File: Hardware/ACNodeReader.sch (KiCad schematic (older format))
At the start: 36 parts, among them J1 8P8C, J2 AVR-ISP-6, J3 Conn_01x04_Female, J4 Conn_01x03_Male, J5 Conn_01x04_Female, J6 Conn_01x03_Male, J7 Conn_01x05_Male, J8 Conn_01x03_Male, SW1 SW_Push, SW2 SW_Push, U1 L78L05_SOT89, U2 ATmega88-20AU, U3 ISL8489EIBZ, U4 SI7060-B-00-IV, Y1 16MHz

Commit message: Update a component value
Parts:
- R11: value R -> 10K
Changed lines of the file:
@@
 P 3650 6000
 F 0 "R11" V 3443 6000 50  0000 C CNN
-F 1 "R" V 3534 6000 50  0000 C CNN
+F 1 "10K" V 3534 6000 50  0000 C CNN
 F 2 "Resistor_SMD:R_0603_1608Metric" V 3580 6000 50  0001 C CNN
 F 3 "~" H 3650 6000 50  0001 C CNN

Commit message: Random locl changes
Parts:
- removed J4, J6, J8: Conn_01x03_Male, Connector_PinHeader_2.54mm:PinHeader_1x03_P2.54mm_Vertical, symbol Connector:Conn_01x03_Male
- removed J7: Conn_01x05_Male, Connector_PinHeader_2.54mm:PinHeader_1x05_P2.54mm_Vertical, symbol Connector:Conn_01x05_Male
- removed R10, R8, R9: 220R, Resistor_SMD:R_0603_1608Metric, symbol Device:R
- removed SW1: SW_Push, Button_Switch_THT:SW_PUSH_6mm, symbol Switch:SW_Push
- removed U2: ATmega88-20AU, Package_QFP:TQFP-32_7x7mm_P0.8mm, symbol MCU_Microchip_ATmega:ATmega88-20AU
- removed Y1: 16MHz, Crystal:Crystal_SMD_HC49-SD, symbol Device:Crystal_Small
- added U2: ATmega88PB-AU, Package_QFP:TQFP-32_7x7mm_P0.8mm, symbol MCU_Microchip_ATmega:ATmega88PB-AU
- added Y1: Crystal_GND24, Crystal:Crystal_SMD_Abracon_ABM3B-4Pin_5.0x3.2mm, symbol Device:Crystal_GND24
- J2: footprint Connector_IDC:IDC-Header_2x03_P2.54mm_Vertical -> Tag-Connect:TC2030-MCP
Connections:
- wire segments 189 -> 157
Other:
- note removed: "I2C Debug"
- note removed: "Power Debug"
- note removed: "Reset Switch"
- note removed: "SPI debug"
- note removed: "Serial Debug"

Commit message: Toying with the circuit a bit
Removed the capacitor across reset since it breaks DebugWire which
is worth having usable because it helps when all hell breaks loose :-)

Added zero ohm links for switching LED from common anode to common cathode

Switched capacitors to (much smaller) MLCC variants in preparation for attempting
to cram everything into a smaller board
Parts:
- removed C1, C2: 470u, Capacitor_SMD:CP_Elec_8x10, symbol Device:CP
- removed C7: 4.7nF, Capacitor_SMD:C_0603_1608Metric, symbol Device:C
- added C1, C2: 10u, Capacitor_SMD:C_0805_2012Metric, symbol Device:C
- added R8: DNF, Resistor_SMD:R_0603_1608Metric, symbol Device:R
- added R9: 0R, Resistor_SMD:R_0603_1608Metric, symbol Device:R
- J2: symbol Connector:AVR-ISP-6 -> ACNodeReader-rescue:AVR-ISP-6-Connector
- U2: symbol MCU_Microchip_ATmega:ATmega88PB-AU -> ACNodeReader-rescue:ATmega88PB-AU-MCU_Microchip_ATmega
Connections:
- wire segments 157 -> 158
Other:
- moved on the sheet: R4
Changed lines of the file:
@@
 EESchema Schematic File Version 4
-LIBS:ACNodeReader-cache
-EELAYER 29 0
+EELAYER 30 0
 EELAYER END
 $Descr A4 11693 8268
@@
 Wire Wire Line
 	2050 1800 2050 1500
-$Comp
-L Device:CP C1
-U 1 1 5D3DABEB
-P 1300 1350
-F 0 "C1" H 1418 1396 50  0000 L CNN
-F 1 "470u" H 1418 1305 50  0000 L CNN
-F 2 "Capacitor_SMD:CP_Elec_8x10" H 1338 1200 50  0001 C CNN
-F 3 "~" H 1300 1350 50  0001 C CNN
-	1    1300 1350
-	1    0    0    -1
-$EndComp
-$Comp
-L Device:CP C2
-U 1 1 5D3DC471
-P 2750 1350
-F 0 "C2" H 2868 1396 50  0000 L CNN
-F 1 "470u" H 2868 1305 50  0000 L CNN
-F 2 "Capacitor_SMD:CP_Elec_8x10" H 2788 1200 50  0001 C CNN
-F 3 "~" H 2750 1350 50  0001 C CNN
-	1    2750 1350
-	1    0    0    -1
-$EndComp
 Wire Wire Line
 	2750 1200 2750 1150
@@
 L power:+5V #PWR0112
 U 1 1 5D3FCC1C
-P 5350 3400
-F 0 "#PWR0112" H 5350 3250 50  0001 C CNN
-F 1 "+5V" H 5450 3450 50  0000 C CNN
-F 2 "" H 5350 3400 50  0001 C CNN
-F 3 "" H 5350 3400 50  0001 C CNN
-	1    5350 3400
+P 5650 3850
+F 0 "#PWR0112" H 5650 3700 50  0001 C CNN
+F 1 "+5V" H 5750 3900 50  0000 C CNN
+F 2 "" H 5650 3850 50  0001 C CNN
+F 3 "" H 5650 3850 50  0001 C CNN
+	1    5650 3850
 	1    0    0    -1
 $EndComp
@@
 $EndComp
 Wire Wire Line
-	6150 3800 6050 3800
+	6150 3800 6100 3800
 $Comp
 L Device:C C5
@@
 L Device:R R4
 U 1 1 5D47849B
-P 5350 3700
-F 0 "R4" H 5420 3746 50  0000 L CNN
-F 1 "10k" H 5420 3655 50  0000 L CNN
-F 2 "Resistor_SMD:R_0805_2012Metric" V 5280 3700 50  0001 C CNN
-F 3 "~" H 5350 3700 50  0001 C CNN
-	1    5350 3700
-	1    0    0    -1
-$EndComp
-Wire Wire Line
-	5350 3950 5350 3850
-Wire Wire Line
-	5350 3550 5350 3400
+P 5500 3950
+F 0 "R4" H 5570 3996 50  0000 L CNN
+F 1 "10k" H 5570 3905 50  0000 L CNN
+F 2 "Resistor_SMD:R_0805_2012Metric" V 5430 3950 50  0001 C CNN
+F 3 "~" H 5500 3950 50  0001 C CNN
+	1    5500 3950
+	0    1    1    0
+$EndComp
 Wire Wire Line
 	5100 3000 5100 2800
@@
 	5750 2800 5750 2950
 Wire Wire Line
-	5750 2950 6050 2950
-Wire Wire Line
-	6050 2950 6050 3800
+	6100 2950 6100 3800
 Connection ~ 5750 2950
 Wire Wire Line
 	5750 2950 5750 3150
-Connection ~ 6050 3800
-Wire Wire Line
-	6050 3800 5900 3800
-Wire Wire Line
-	5450 3950 5350 3950
-Connection ~ 5350 3950
-Wire Wire Line
-	5750 3950 5750 3800
-Wire Wire Line
-	5750 3800 5900 3800
 Connection ~ 5900 3800
 $Comp
-L Device:C C7
-U 1 1 5D4A17E0
-P 5600 3950
-F 0 "C7" V 5450 3950 50  0000 C CNN
-F 1 "4.7nF" V 5750 3950 50  0000 C CNN
-F 2 "Capacitor_SMD:C_0603_1608Metric" H 5638 3800 50  0001 C CNN
-F 3 "~" H 5600 3950 50  0001 C CNN
-	1    5600 3950
-	0    1    1    0
-$EndComp
-$Comp
-L Connector:AVR-ISP-6 J2
+L ACNodeReader-rescue:AVR-ISP-6-Connector J2
 U 1 1 5D4A869B
 P 5300 2100
@@
 U 1 1 5D569267
 P 5150 3450
-F 0 "J5" H 5178 3426 50  0000 L CNN
-F 1 "Conn_01x04_Female" H 5178 3335 50  0000 L CNN
+F 0 "J5" H 5150 3300 50  0000 L CNN
+F 1 "Conn_01x04_Female" H 4850 3200 50  0000 L CNN
 F 2 "Connector_PinHeader_2.54mm:PinHeader_1x04_P2.54mm_Vertical" H 5150 3450 50  0001 C CNN
 F 3 "~" H 5150 3450 50  0001 C CNN
@@
 	4150 3600 4350 3600
 Wire Wire Line
-	5900 3250 5900 3800
+	5900 3250 5900 3400
 Wire Wire Line
 	4950 3450 4850 3450
@@
 	2350 1150 2750 1150
 $Comp
-L MCU_Microchip_ATmega:ATmega88PB-AU U2
+L ACNodeReader-rescue:ATmega88PB-AU-MCU_Microchip_ATmega U2
 U 1 1 5D98CB6F
 P 3450 3650
@@
 $EndComp
 Wire Wire Line
-	4850 3250 5900 3250
+	4850 3250 5700 3250
 Wire Wire Line
 	4050 3050 4300 3050
@@
 Wire Wire Line
 	4350 3100 4750 3100
+Wire Wire Line
+	5650 3950 5650 3850
+$Comp
+L Device:R R9
+U 1 1 5EE364C3
+P 5900 3550
+F 0 "R9" H 5830 3504 50  0000 R CNN
+F 1 "0R" H 5830 3595 50  0000 R CNN
+F 2 "Resistor_SMD:R_0603_1608Metric" V 5830 3550 50  0001 C CNN
+F 3 "~" H 5900 3550 50  0001 C CNN
+	1    5900 3550
+	-1   0    0    1
+$EndComp
+Wire Wire Line
+	5900 3700 5900 3800
+$Comp
+L Device:R R8
+U 1 1 5EE3ACF5
+P 5700 3550
+F 0 "R8" H 5550 3600 50  0000 L CNN
+F 1 "DNF" H 5500 3500 50  0000 L CNN
+F 2 "Resistor_SMD:R_0603_1608Metric" V 5630 3550 50  0001 C CNN
+F 3 "~" H 5700 3550 50  0001 C CNN
+	1    5700 3550
+	1    0    0    -1
+$EndComp
+Wire Wire Line
+	5700 3400 5700 3250
+Connection ~ 5700 3250
+Wire Wire Line
+	5700 3250 5900 3250
+Wire Wire Line
+	5700 3700 5700 3950
+Wire Wire Line
+	5700 3950 5650 3950
+Connection ~ 5650 3950
+Connection ~ 6100 3800
+Wire Wire Line
+	5900 3800 6100 3800
+Wire Wire Line
+	5750 2950 6100 2950
+$Comp
+L Device:C C1
+U 1 1 5EE74DE3
+P 1300 1350
+F 0 "C1" H 1415 1396 50  0000 L CNN
+F 1 "10u" H 1415 1305 50  0000 L CNN
+F 2 "Capacitor_SMD:C_0805_2012Metric" H 1338 1200 50  0001 C CNN
+F 3 "~" H 1300 1350 50  0001 C CNN
+	1    1300 1350
+	1    0    0    -1
+$EndComp
+$Comp
+L Device:C C2
+U 1 1 5EE7545C
+P 2750 1350
+F 0 "C2" H 2865 1396 50  0000 L CNN
+F 1 "10u" H 2865 1305 50  0000 L CNN
+F 2 "Capacitor_SMD:C_0805_2012Metric" H 2788 1200 50  0001 C CNN
+F 3 "~" H 2750 1350 50  0001 C CNN
+	1    2750 1350
+	1    0    0    -1
+$EndComp
 $EndSCHEMATC

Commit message: New, smaller, better PCB design
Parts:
- removed J1: 8P8C, Connector_RJ:RJ45_Amphenol_54602-x08_Horizontal, symbol Connector:8P8C
- removed SW2: SW_Push, Button_Switch_THT:SW_PUSH_6mm, symbol Switch:SW_Push
- removed U4: SI7060-B-00-IV, Package_TO_SOT_SMD:SOT-23-5, symbol ExtraParts:SI7060-B-00-IV
- added D1: D_Zener, Diode_SMD:D_SOD-323F, symbol Device:D_Zener
- added H1, H2: MountingHole, MountingHole:MountingHole_3.2mm_M3_DIN965, symbol Mechanical:MountingHole
- added J1: Conn_01x08_Male, Connector_PinHeader_2.54mm:PinHeader_1x08_P2.54mm_Horizontal, symbol Connector:Conn_01x08_Male
- added J4: Conn_01x02_Male, Connector_PinHeader_2.54mm:PinHeader_1x02_P2.54mm_Horizontal, symbol Connector:Conn_01x02_Male
- added J6: Conn_01x04_Male, Connector_PinHeader_2.54mm:PinHeader_1x04_P2.54mm_Horizontal, symbol Connector:Conn_01x04_Male
- added J7: Conn_01x04_Male, Connector_PinHeader_2.54mm:PinHeader_1x04_P2.54mm_Vertical, symbol Connector:Conn_01x04_Male
- added U4: LM75C, Package_SO:SO-8_3.9x4.9mm_P1.27mm, symbol Sensor_Temperature:LM75C
- J2: footprint Tag-Connect:TC2030-MCP -> Tag-Connect:TC2030-MCP-NL
- J5: footprint Connector_PinHeader_2.54mm:PinHeader_1x04_P2.54mm_Vertical -> Connector_PinHeader_2.54mm:PinHeader_1x04_P2.54mm_Horizontal
- R1, R2, R4: footprint Resistor_SMD:R_0805_2012Metric -> Resistor_SMD:R_0603_1608Metric
- Y1: footprint Crystal:Crystal_SMD_Abracon_ABM3B-4Pin_5.0x3.2mm -> Crystal:Crystal_SMD_7050-4Pin_7.0x5.0mm
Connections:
- net +12V: now also D1.1 (K), J1.4 (Pin_4), J1.5 (Pin_5)
- net +5V: now also R9.1, J6.3 (Pin_3), J7.1 (Pin_1), U4.8 (+Vs); no longer R8.2
- net GND: now also R8.2, D1.2 (A), J1.1 (Pin_1), J1.2 (Pin_2), J6.4 (Pin_4), J7.2 (Pin_2), U4.4 (GND), U4.5 (A2), U4.6 (A1), U4.7 (A0); no longer R9.1
- net RX+: now also J1.8 (Pin_8)
- net RX-: now also J1.7 (Pin_7)
- net TX+: now also J1.6 (Pin_6)
- net TX-: now also J1.3 (Pin_3)
- net i2c_SCL: now also R1.1, J7.3 (Pin_3), U4.2 (SCL); no longer R2.1
- net i2c_SDA: now also R2.1, J7.4 (Pin_4), U4.1 (SDA); no longer R1.1
- net uC_RX: now also J6.2 (Pin_2)
- net uC_TX: now also J6.1 (Pin_1)
- net at U2.23 (PC0): no longer R5.2
- net at U2.24 (PC1): no longer R6.2
- net at U2.25 (PC2): no longer R7.2
- net at C10.2, R11.1: now also J4.2 (Pin_2)
- net at C10.1, U2.11 (PD7): now also J4.1 (Pin_1)
- net LED2: now reaches U2.10 (PD6)
- net LED2: now also R6.2
- net LED3: now reaches U2.13 (PB1)
- net LED3: now also R7.2
- net LED1: now reaches U2.9 (PD5)
- net LED1: now also R5.2
- no-connect marks 1 -> 13
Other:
- note added: "May be TMP1075, PCT2075 or any other LM75-compatible IC"
- moved on the sheet: C9, J5, R1, R2, R5, R6, R7, R8, R9

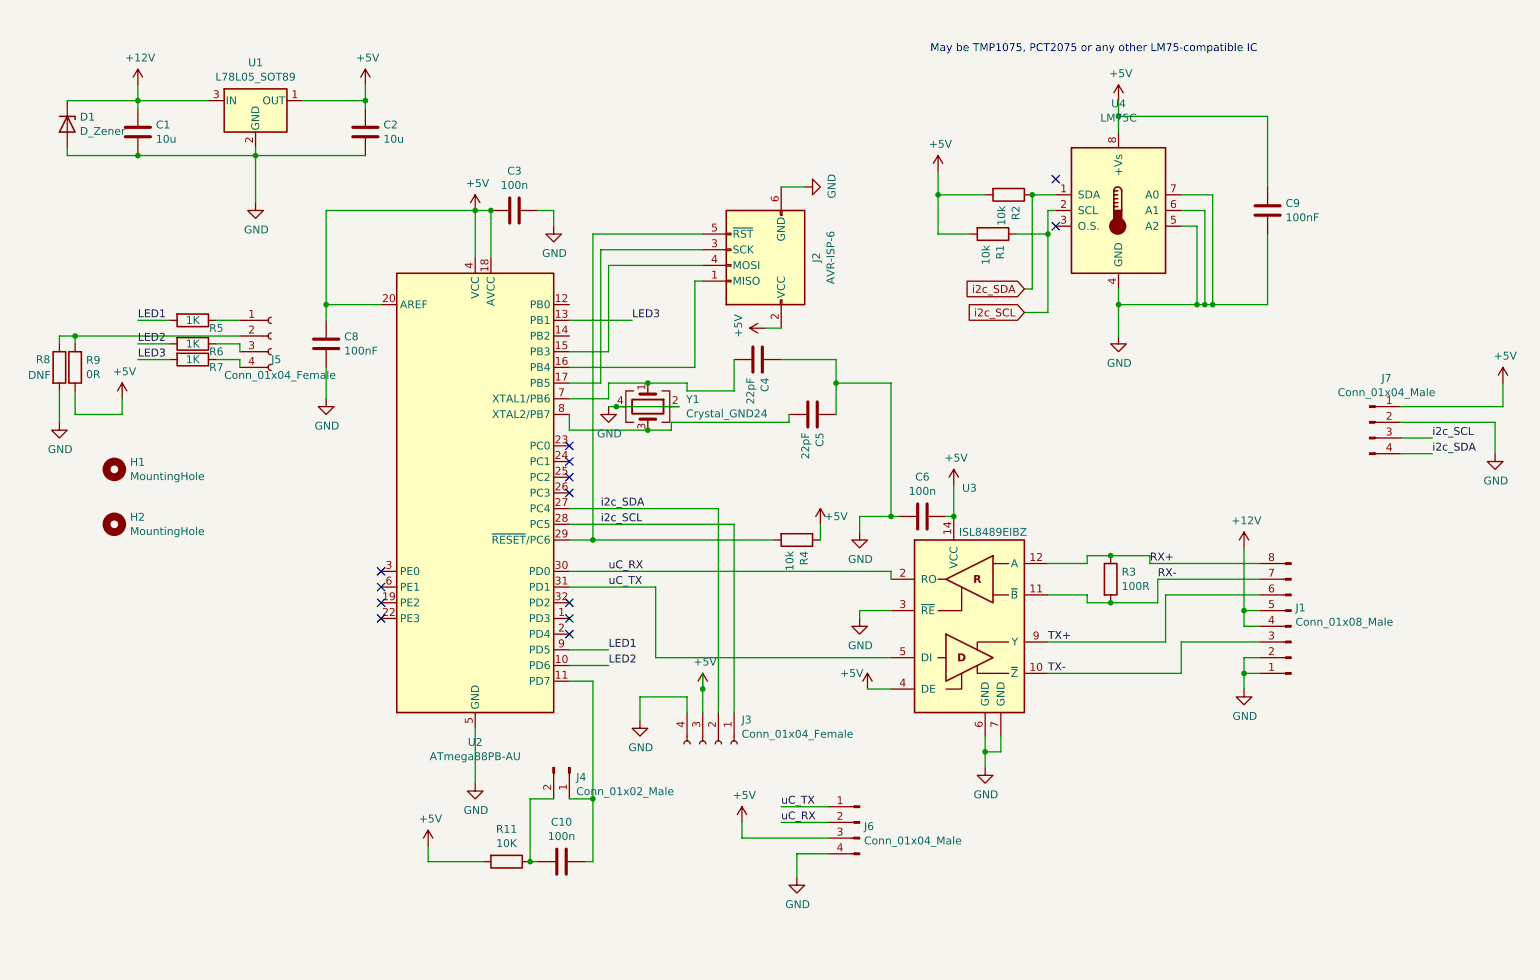
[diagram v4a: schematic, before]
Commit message: Slight schematic changes - mostly text descriptions
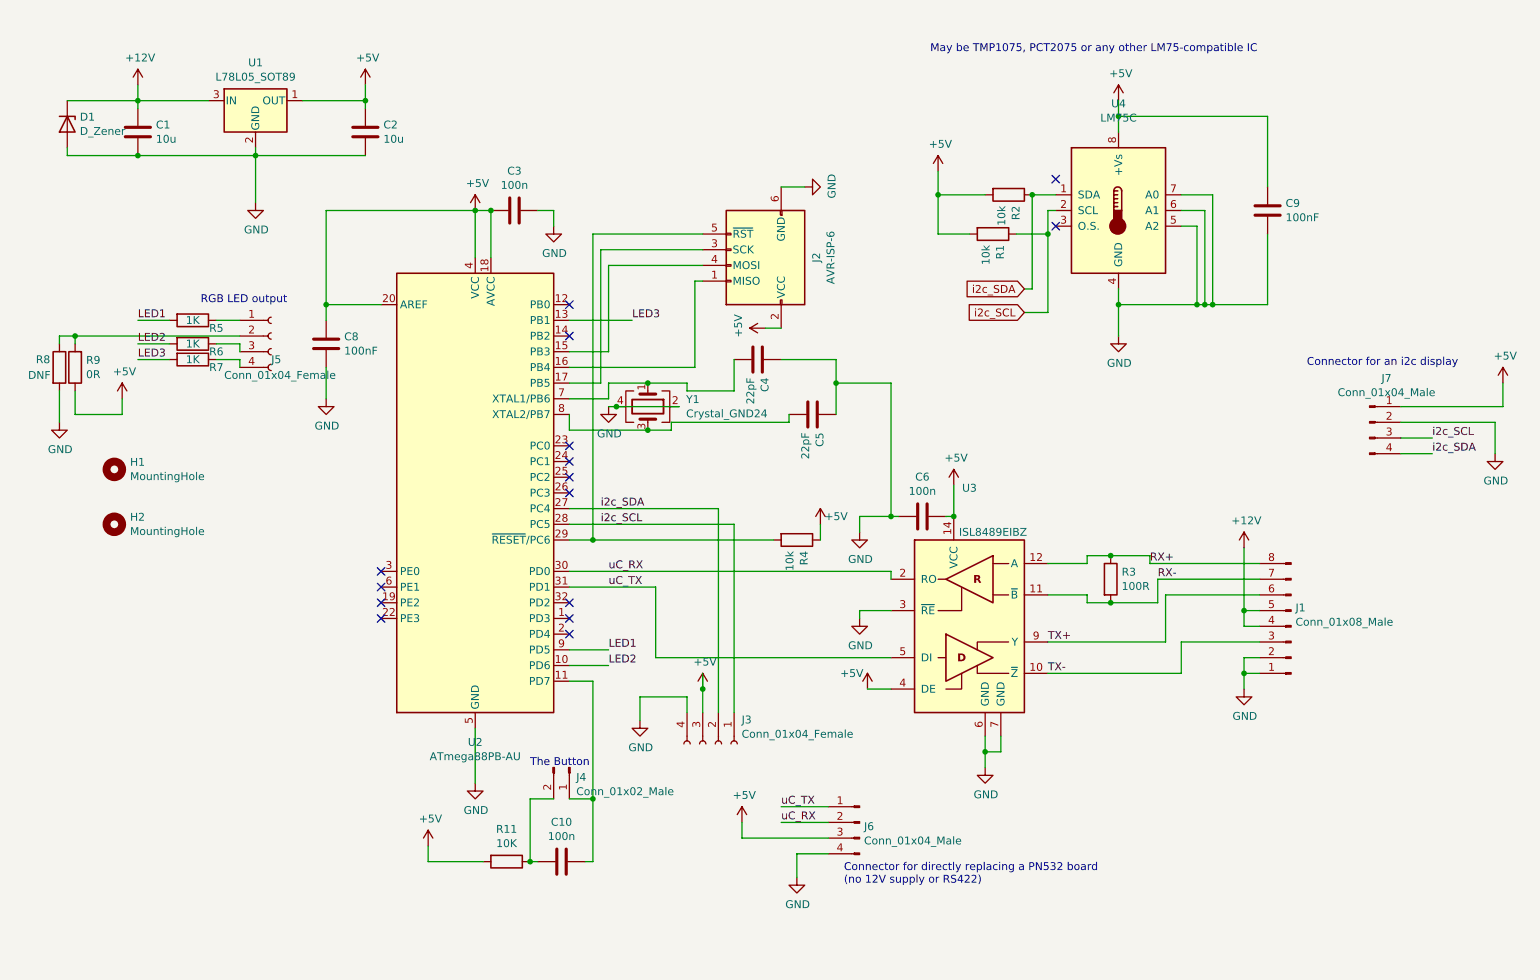
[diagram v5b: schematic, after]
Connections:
- no-connect marks 13 -> 15
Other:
- note added: "Connector for an i2c display"
- note added: "Connector for directly replacing a PN532 board\n(no 12V supply or RS422)"
- note added: "RGB LED output"
- note added: "The Button"
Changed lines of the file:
@@
 Wire Wire Line
 	9350 3200 9950 3200
+Text Notes 8750 2850 0    50   ~ 0
+Connector for an i2c display
+Text Notes 5800 6150 0    50   ~ 0
+Connector for directly replacing a PN532 board\n(no 12V supply or RS422)
+Text Notes 3800 5400 0    50   ~ 0
+The Button
+Text Notes 1700 2450 0    50   ~ 0
+RGB LED output
+NoConn ~ 4050 2450
+NoConn ~ 4050 2650
 $EndSCHEMATC

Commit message: Added some notes to schematic and updated firmware with new board support
getting there!
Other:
- note added: "Could also use AP7381-50Y-13 (150mA max current)\nOr AP2205-50YR-13 (200mA)\nMaybe redesign to support MCP1700/2/3 on later version (for 250mA max current)?\n\nThe PN532 probably pulls more than 100mA (and maybe more than 150mA)\n"
- note added: "Don't forget these capacitors lose\ncapacitance as the voltage rises!\n\nSuggest 25V rating or more\n"
- moved on the sheet: C1, C2, D1, U1
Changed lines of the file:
@@
 L Regulator_Linear:L78L05_SOT89 U1
 U 1 1 5D3D7904
-P 2050 1150
-F 0 "U1" H 2050 1392 50  0000 C CNN
-F 1 "L78L05_SOT89" H 2050 1301 50  0000 C CNN
-F 2 "Package_TO_SOT_SMD:SOT-89-3" H 2050 1350 50  0001 C CIN
-F 3 "http://www.st.com/content/ccc/resource/technical/document/datasheet/15/55/e5/aa/23/5b/43/fd/CD00000446.pdf/files/CD00000446.pdf/jcr:content/translations/en.CD00000446.pdf" H 2050 1100 50  0001 C CNN
-	1    2050 1150
+P 1950 1350
+F 0 "U1" H 1950 1592 50  0000 C CNN
+F 1 "L78L05_SOT89" H 1950 1501 50  0000 C CNN
+F 2 "Package_TO_SOT_SMD:SOT-89-3" H 1950 1550 50  0001 C CIN
+F 3 "http://www.st.com/content/ccc/resource/technical/document/datasheet/15/55/e5/aa/23/5b/43/fd/CD00000446.pdf/files/CD00000446.pdf/jcr:content/translations/en.CD00000446.pdf" H 1950 1300 50  0001 C CNN
+	1    1950 1350
 	1    0    0    -1
 $EndComp
@@
 L power:GND #PWR0103
 U 1 1 5D3D8510
-P 2050 1800
-F 0 "#PWR0103" H 2050 1550 50  0001 C CNN
-F 1 "GND" H 2055 1627 50  0000 C CNN
-F 2 "" H 2050 1800 50  0001 C CNN
-F 3 "" H 2050 1800 50  0001 C CNN
-	1    2050 1800
+P 1950 2000
+F 0 "#PWR0103" H 1950 1750 50  0001 C CNN
+F 1 "GND" H 1955 1827 50  0000 C CNN
+F 2 "" H 1950 2000 50  0001 C CNN
+F 3 "" H 1950 2000 50  0001 C CNN
+	1    1950 2000
 	1    0    0    -1
 $EndComp
@@
 L power:+12V #PWR0104
 U 1 1 5D3D8CA0
-P 1300 1050
-F 0 "#PWR0104" H 1300 900 50  0001 C CNN
-F 1 "+12V" H 1315 1223 50  0000 C CNN
-F 2 "" H 1300 1050 50  0001 C CNN
-F 3 "" H 1300 1050 50  0001 C CNN
-	1    1300 1050
+P 1200 1250
+F 0 "#PWR0104" H 1200 1100 50  0001 C CNN
+F 1 "+12V" H 1215 1423 50  0000 C CNN
+F 2 "" H 1200 1250 50  0001 C CNN
+F 3 "" H 1200 1250 50  0001 C CNN
+	1    1200 1250
 	1    0    0    -1
 $EndComp
@@
 L power:+5V #PWR0105
 U 1 1 5D3D9614
-P 2750 1050
-F 0 "#PWR0105" H 2750 900 50  0001 C CNN
-F 1 "+5V" H 2765 1223 50  0000 C CNN
-F 2 "" H 2750 1050 50  0001 C CNN
-F 3 "" H 2750 1050 50  0001 C CNN
-	1    2750 1050
-	1    0    0    -1
-$EndComp
-Wire Wire Line
-	1300 1050 1300 1150
-Wire Wire Line
-	2750 1150 2750 1050
-Wire Wire Line
-	2050 1800 2050 1500
-Wire Wire Line
-	2750 1200 2750 1150
-Connection ~ 2750 1150
-Wire Wire Line
-	2750 1500 2050 1500
-Connection ~ 2050 1500
-Wire Wire Line
-	2050 1500 2050 1450
-Wire Wire Line
-	1300 1200 1300 1150
-Connection ~ 1300 1150
+P 2650 1250
+F 0 "#PWR0105" H 2650 1100 50  0001 C CNN
+F 1 "+5V" H 2665 1423 50  0000 C CNN
+F 2 "" H 2650 1250 50  0001 C CNN
+F 3 "" H 2650 1250 50  0001 C CNN
+	1    2650 1250
+	1    0    0    -1
+$EndComp
+Wire Wire Line
+	1200 1250 1200 1350
+Wire Wire Line
+	2650 1350 2650 1250
+Wire Wire Line
+	1950 2000 1950 1700
+Wire Wire Line
+	2650 1400 2650 1350
+Connection ~ 2650 1350
+Connection ~ 1950 1700
+Wire Wire Line
+	1950 1700 1950 1650
+Wire Wire Line
+	1200 1400 1200 1350
+Connection ~ 1200 1350
 Wire Wire Line
 	4050 4250 4600 4250
@@
 i2c_SDA
 Wire Wire Line
-	1300 1150 1750 1150
-Wire Wire Line
-	1300 1500 2050 1500
-Wire Wire Line
-	2350 1150 2750 1150
+	1200 1350 1650 1350
+Wire Wire Line
+	1200 1700 1950 1700
+Wire Wire Line
+	2250 1350 2650 1350
 $Comp
 L ACNodeReader-rescue:ATmega88PB-AU-MCU_Microchip_ATmega U2
@@
 L Device:C C1
 U 1 1 5EE74DE3
-P 1300 1350
-F 0 "C1" H 1415 1396 50  0000 L CNN
-F 1 "10u" H 1415 1305 50  0000 L CNN
-F 2 "Capacitor_SMD:C_0805_2012Metric" H 1338 1200 50  0001 C CNN
-F 3 "~" H 1300 1350 50  0001 C CNN
-	1    1300 1350
+P 1200 1550
+F 0 "C1" H 1315 1596 50  0000 L CNN
+F 1 "10u" H 1315 1505 50  0000 L CNN
+F 2 "Capacitor_SMD:C_0805_2012Metric" H 1238 1400 50  0001 C CNN
+F 3 "~" H 1200 1550 50  0001 C CNN
+	1    1200 1550
 	1    0    0    -1
 $EndComp
@@
 L Device:C C2
 U 1 1 5EE7545C
-P 2750 1350
-F 0 "C2" H 2865 1396 50  0000 L CNN
-F 1 "10u" H 2865 1305 50  0000 L CNN
-F 2 "Capacitor_SMD:C_0805_2012Metric" H 2788 1200 50  0001 C CNN
-F 3 "~" H 2750 1350 50  0001 C CNN
-	1    2750 1350
+P 2650 1550
+F 0 "C2" H 2765 1596 50  0000 L CNN
+F 1 "10u" H 2765 1505 50  0000 L CNN
+F 2 "Capacitor_SMD:C_0805_2012Metric" H 2688 1400 50  0001 C CNN
+F 3 "~" H 2650 1550 50  0001 C CNN
+	1    2650 1550
 	1    0    0    -1
 $EndComp
@@
 L Device:D_Zener D1
 U 1 1 5F745A0A
-P 850 1300
-F 0 "D1" V 804 1380 50  0000 L CNN
-F 1 "D_Zener" V 895 1380 50  0000 L CNN
-F 2 "Diode_SMD:D_SOD-323F" H 850 1300 50  0001 C CNN
-F 3 "~" H 850 1300 50  0001 C CNN
-	1    850  1300
-	0    1    1    0
-$EndComp
-Wire Wire Line
-	1300 1150 850  1150
-Wire Wire Line
-	1300 1500 850  1500
-Wire Wire Line
-	850  1500 850  1450
-Connection ~ 1300 1500
+P 750 1500
+F 0 "D1" V 704 1580 50  0000 L CNN
+F 1 "D_Zener" V 795 1580 50  0000 L CNN
+F 2 "Diode_SMD:D_SOD-323F" H 750 1500 50  0001 C CNN
+F 3 "~" H 750 1500 50  0001 C CNN
+	1    750  1500
+	0    1    1    0
+$EndComp
+Wire Wire Line
+	1200 1350 750  1350
+Wire Wire Line
+	1200 1700 750  1700
+Wire Wire Line
+	750  1700 750  1650
+Connection ~ 1200 1700
 Wire Wire Line
 	4600 4700 6100 4700
@@
 NoConn ~ 4050 2450
 NoConn ~ 4050 2650
+Text Notes 650  1000 0    50   ~ 0
+Could also use AP7381-50Y-13 (150mA max current)\nOr AP2205-50YR-13 (200mA)\nMaybe redesign to support MCP1700/2/3 on later version (for 250mA max current)?\n\nThe PN532 probably pulls more than 100mA (and maybe more than 150mA)\n
+Wire Wire Line
+	1950 1700 2650 1700
+Text Notes 600  2050 0    50   ~ 0
+Don't forget these capacitors lose\ncapacitance as the voltage rises!\n\nSuggest 25V rating or more\n
 $EndSCHEMATC
